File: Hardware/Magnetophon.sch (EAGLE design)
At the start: 22 parts, among them U2 TL072_

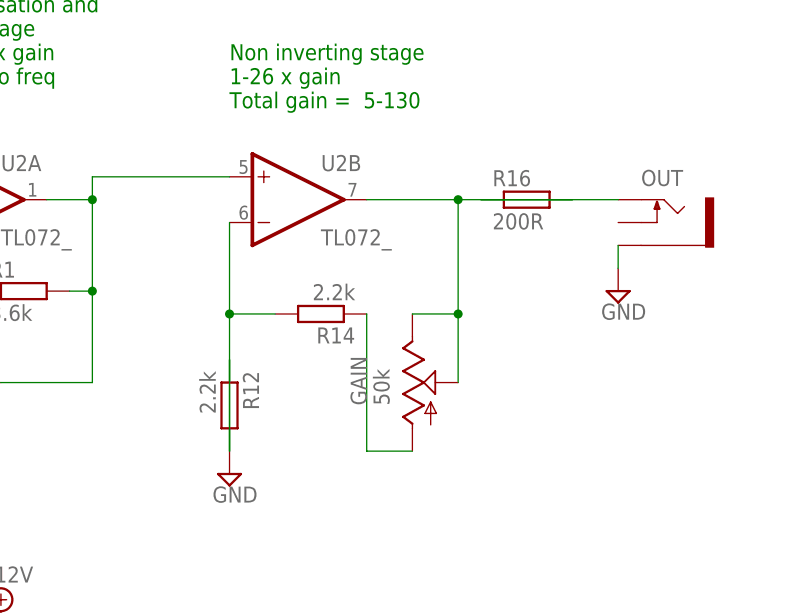
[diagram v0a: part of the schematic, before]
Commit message: Add via to ground panel artwork
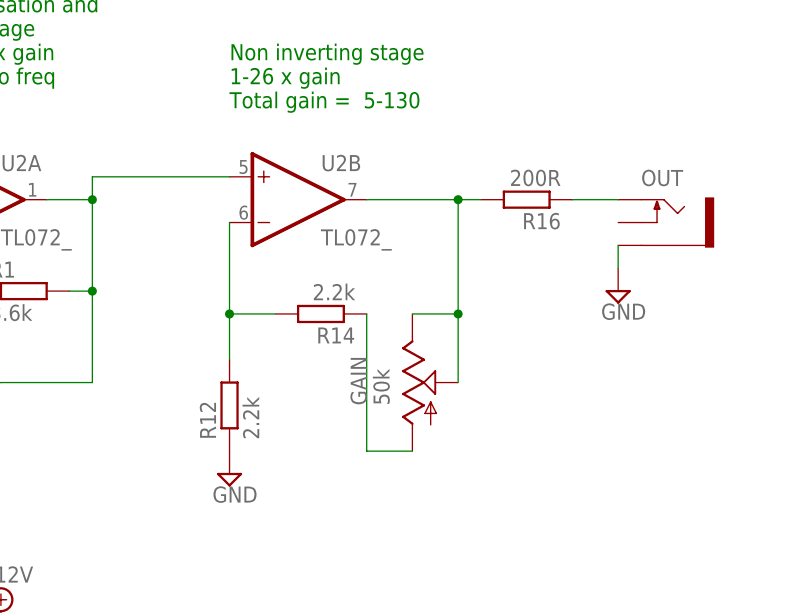
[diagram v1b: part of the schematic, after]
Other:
- moved on the sheet: R12, R16
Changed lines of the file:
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@@
 <?xml version="1.0" encoding="utf-8"?>
 <!DOCTYPE eagle SYSTEM "eagle.dtd">
-<eagle version="7.2.0">
+<eagle version="7.4.0">
 <drawing>
 <settings>
@@
 <instance part="SUPPLY3" gate="GND" x="66.04" y="109.22"/>
 <instance part="R14" gate="G$1" x="167.64" y="114.3" rot="R180"/>
-<instance part="R16" gate="G$1" x="190.5" y="127"/>
+<instance part="R16" gate="G$1" x="190.5" y="127" rot="R180"/>
 <instance part="SUPPLY7" gate="GND" x="200.66" y="116.84"/>
 <instance part="R8" gate="G$1" x="116.84" y="99.06" rot="R270"/>
 <instance part="R10" gate="G$1" x="127" y="106.68"/>
 <instance part="SUPPLY9" gate="GND" x="116.84" y="78.74"/>
-<instance part="R12" gate="G$1" x="157.48" y="104.14" rot="R270"/>
+<instance part="R12" gate="G$1" x="157.48" y="104.14" rot="R90"/>
 <instance part="SUPPLY5" gate="GND" x="157.48" y="96.52"/>
 <instance part="GND21" gate="1" x="111.76" y="63.5"/>
@@
 <pinref part="R12" gate="G$1" pin="1"/>
 <pinref part="SUPPLY5" gate="GND" pin="GND"/>
-<wire x1="157.48" y1="99.06" x2="157.48" y2="109.22" width="0.1524" layer="91"/>
 </segment>
 <segment>
@@
 <segment>
 <pinref part="U2" gate="B" pin="OUT"/>
-<wire x1="195.58" y1="127" x2="182.88" y2="127" width="0.1524" layer="91"/>
+<wire x1="185.42" y1="127" x2="182.88" y2="127" width="0.1524" layer="91"/>
 <wire x1="182.88" y1="127" x2="172.72" y2="127" width="0.1524" layer="91"/>
 <pinref part="R16" gate="G$1" pin="2"/>
@@
 <segment>
 <pinref part="R16" gate="G$1" pin="1"/>
-<wire x1="200.66" y1="127" x2="185.42" y2="127" width="0.1524" layer="91"/>
+<wire x1="200.66" y1="127" x2="195.58" y2="127" width="0.1524" layer="91"/>
 <pinref part="OUT" gate="G$1" pin="TIP"/>
 </segment>
@@
 <pinref part="R12" gate="G$1" pin="2"/>
 <pinref part="R14" gate="G$1" pin="2"/>
-<wire x1="157.48" y1="114.3" x2="157.48" y2="99.06" width="0.1524" layer="91"/>
+<wire x1="157.48" y1="114.3" x2="157.48" y2="109.22" width="0.1524" layer="91"/>
 <wire x1="162.56" y1="114.3" x2="157.48" y2="114.3" width="0.1524" layer="91"/>
 <junction x="157.48" y="114.3"/>
